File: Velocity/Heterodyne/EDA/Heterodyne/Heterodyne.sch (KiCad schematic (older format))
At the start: 35 parts, among them J3 PWR, J4 Doppler_Out, J5 V_Square, J6 OP_OUT, J7 Reciever, J8 Emmiter, U1 SA612AD, U2 NE5532, U3 MAX7375AXR105

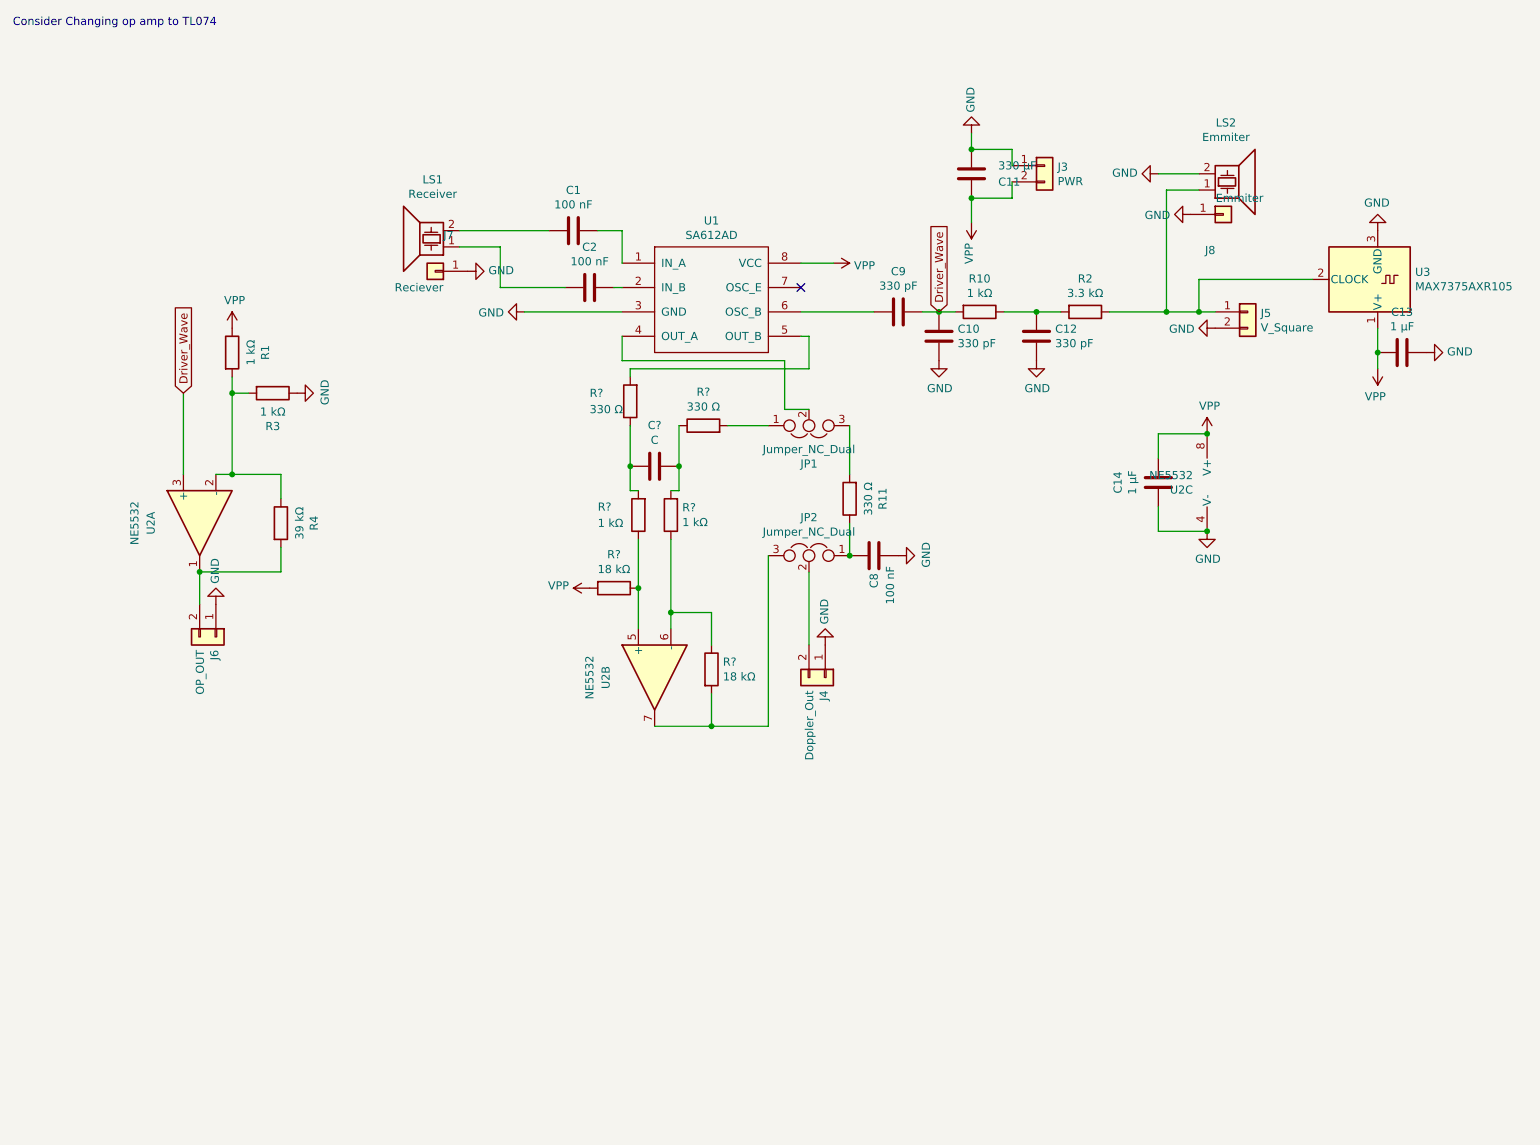
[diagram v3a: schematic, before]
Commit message: updated data to heterodyne pcb to include adc
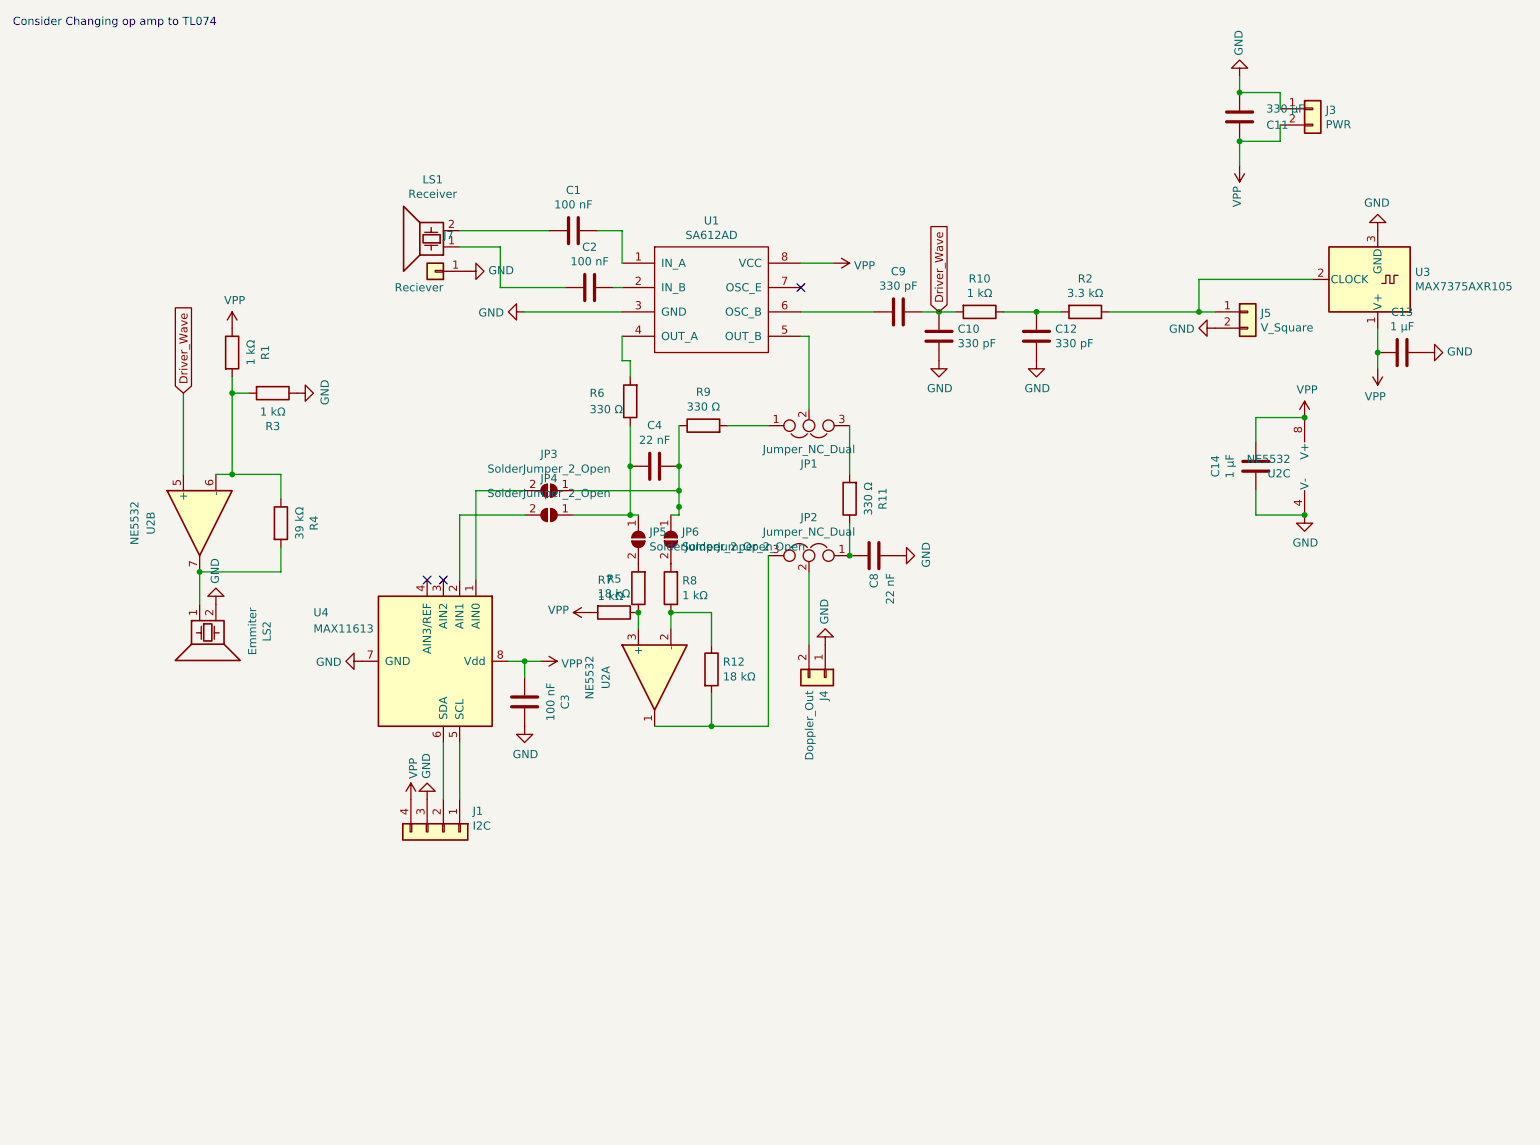
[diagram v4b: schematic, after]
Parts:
- removed J6: OP_OUT, Pin_Headers:Pin_Header_Straight_1x02_Pitch2.54mm, symbol Heterodyne-rescue:Conn_01x02-Connector_Generic
- removed J8: Emmiter, Pin_Headers:Pin_Header_Straight_1x01_Pitch2.54mm, symbol Heterodyne-rescue:Conn_01x01-Connector_Generic
- added C3: 100 nF, Capacitor_SMD:C_0805_2012Metric_Pad1.15x1.40mm_HandSolder, symbol Heterodyne-rescue:C-Device
- added J1: I2C, Connector_PinHeader_2.54mm:PinHeader_1x04_P2.54mm_Vertical, symbol Connector_Generic:Conn_01x04
- added JP3, JP4, JP5, JP6: SolderJumper_2_Open, Jumper:SolderJumper-2_P1.3mm_Open_Pad1.0x1.5mm, symbol Jumper:SolderJumper_2_Open
- added U4: MAX11613, Package_SO:MSOP-8_3x3mm_P0.65mm, symbol Analog_ADC:MAX11613
- C1, C10, C12, C2, C9: footprint Capacitors_SMD:C_0805_HandSoldering -> Capacitor_SMD:C_0805_2012Metric_Pad1.15x1.40mm_HandSolder
- C11: footprint Capacitors_SMD:CP_Elec_8x10 -> Capacitor_SMD:CP_Elec_8x10
- C13, C14: footprint Capacitors_SMD:C_1206_HandSoldering -> Capacitor_SMD:C_1206_3216Metric_Pad1.42x1.75mm_HandSolder
- C4: renamed from C?; value C -> 22 nF; footprint (none) -> Capacitor_SMD:C_0805_2012Metric_Pad1.15x1.40mm_HandSolder
- C8: value 100 nF -> 22 nF; footprint Capacitors_SMD:C_0805_HandSoldering -> Capacitor_SMD:C_0805_2012Metric_Pad1.15x1.40mm_HandSolder
- J3, J4, J5, LS1, LS2: footprint Pin_Headers:Pin_Header_Straight_1x02_Pitch2.54mm -> Connector_PinHeader_2.54mm:PinHeader_1x02_P2.54mm_Vertical
- J7: footprint Pin_Headers:Pin_Header_Straight_1x01_Pitch2.54mm -> Connector_PinSocket_2.54mm:PinSocket_1x01_P2.54mm_Vertical
- JP1, JP2: footprint Connectors:GS3 -> Jumper:SolderJumper-3_P1.3mm_Open_Pad1.0x1.5mm
- R1, R10, R11, R2, R3, R4: footprint Resistors_SMD:R_0805_HandSoldering -> Resistor_SMD:R_0805_2012Metric_Pad1.15x1.40mm_HandSolder
- R12, R5, R6, R7, R8, R9: renamed from R?; footprint (none) -> Resistor_SMD:R_0805_2012Metric_Pad1.15x1.40mm_HandSolder
- U1: footprint Housings_SOIC:SO-8_5.3x6.2mm_Pitch1.27mm -> Package_SO:SOIC-8_5.275x5.275mm_P1.27mm
- U2: footprint Housings_DIP:DIP-8_W7.62mm_LongPads -> Package_DIP:DIP-8_W7.62mm
- U3: footprint TO_SOT_Packages_SMD:SOT-323_SC-70_Handsoldering -> Package_TO_SOT_SMD:SOT-323_SC-70_Handsoldering
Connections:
- net Driver_Wave: now also U2.5 (+); no longer U2.3 (+)
- net GND: now also C3.1, J1.3 (Pin_3), U4.7 (GND)
- net VPP: now also C3.2, J1.4 (Pin_4), U4.8 (Vdd)
- net at U1.4 (OUT_A): now also R6.2; no longer JP1.2
- net at U1.5 (OUT_B): now also JP1.2; no longer R6.2
- net at J5.1 (Pin_1), R2.1, U3.2 (CLOCK): no longer LS2.1
- net at R5.1, R7.1: now also U2.3 (+); no longer U2.5 (+)
- net at R12.1, R8.1: now also U2.2 (-); no longer U2.6 (-)
- net at JP2.3, R12.2: now also U2.1; no longer U2.7
- net at R4.2: now also LS2.1, U2.7; no longer U2.1
- net at R1.2, R3.2, R4.1: now also U2.6 (-); no longer U2.2 (-)
- net at C4.2, R6.1: now also JP4.1 (A), JP5.1 (A); no longer R7.2
- net at C4.1, R9.1: now also JP3.1 (A), JP6.1 (A); no longer R8.2
- new net: JP5.2 (B), R7.2
- new net: JP6.2 (B), R8.2
- new net: JP3.2 (B), U4.1 (AIN0)
- new net: JP4.2 (B), U4.2 (AIN1)
- new net: J1.1 (Pin_1), U4.5 (SCL)
- new net: J1.2 (Pin_2), U4.6 (SDA)
- no-connect marks 1 -> 3
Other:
- moved on the sheet: C11, C14, J3, LS2, R5, R7, R8, U2C

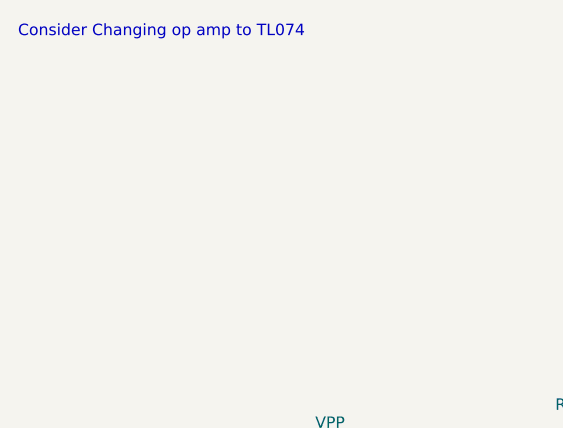
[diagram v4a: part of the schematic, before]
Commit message: calibrated velocity, implemented multi sample rate rangeing
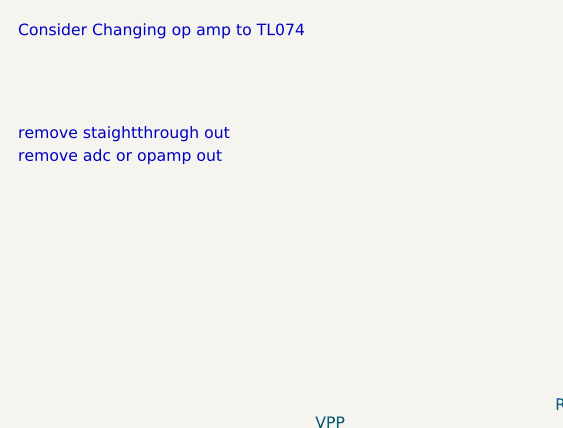
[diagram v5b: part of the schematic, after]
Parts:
- U2: footprint Package_DIP:DIP-8_W7.62mm -> Package_SO:SOIC-8_3.9x4.9mm_P1.27mm
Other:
- note added: "remove adc or opamp out\n"
- note added: "remove staightthrough out"
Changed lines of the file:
@@
 F 0 "U2" H 8863 3455 50  0000 R CNN
 F 1 "NE5532" H 8863 3544 50  0000 R CNN
-F 2 "Package_DIP:DIP-8_W7.62mm" H 9050 3500 50  0001 C CNN
+F 2 "Package_SO:SOIC-8_3.9x4.9mm_P1.27mm" H 9050 3500 50  0001 C CNN
 F 3 "http://www.ti.com/lit/ds/symlink/ne5532.pdf" H 9050 3500 50  0001 C CNN
 	3    9050 3500
@@
 F 0 "U2" H 2150 4150 50  0000 C CNN
 F 1 "NE5532" H 2150 4250 50  0000 C CNN
-F 2 "Package_DIP:DIP-8_W7.62mm" H 2150 3850 50  0001 C CNN
+F 2 "Package_SO:SOIC-8_3.9x4.9mm_P1.27mm" H 2150 3850 50  0001 C CNN
 F 3 "http://www.ti.com/lit/ds/symlink/ne5532.pdf" H 2150 3850 50  0001 C CNN
 	2    2150 3850
@@
 F 0 "U2" H 4950 5100 50  0000 C CNN
 F 1 "NE5532" H 4950 5200 50  0000 C CNN
-F 2 "Package_DIP:DIP-8_W7.62mm" H 4950 4800 50  0001 C CNN
+F 2 "Package_SO:SOIC-8_3.9x4.9mm_P1.27mm" H 4950 4800 50  0001 C CNN
 F 3 "http://www.ti.com/lit/ds/symlink/ne5532.pdf" H 4950 4800 50  0001 C CNN
 	1    4950 4800
@@
 Wire Wire Line
 	5100 3750 5100 3800
+Text Notes 1000 1250 0    50   ~ 0
+remove staightthrough out
+Text Notes 1000 1350 0    50   ~ 0
+remove adc or opamp out\n
 $EndSCHEMATC

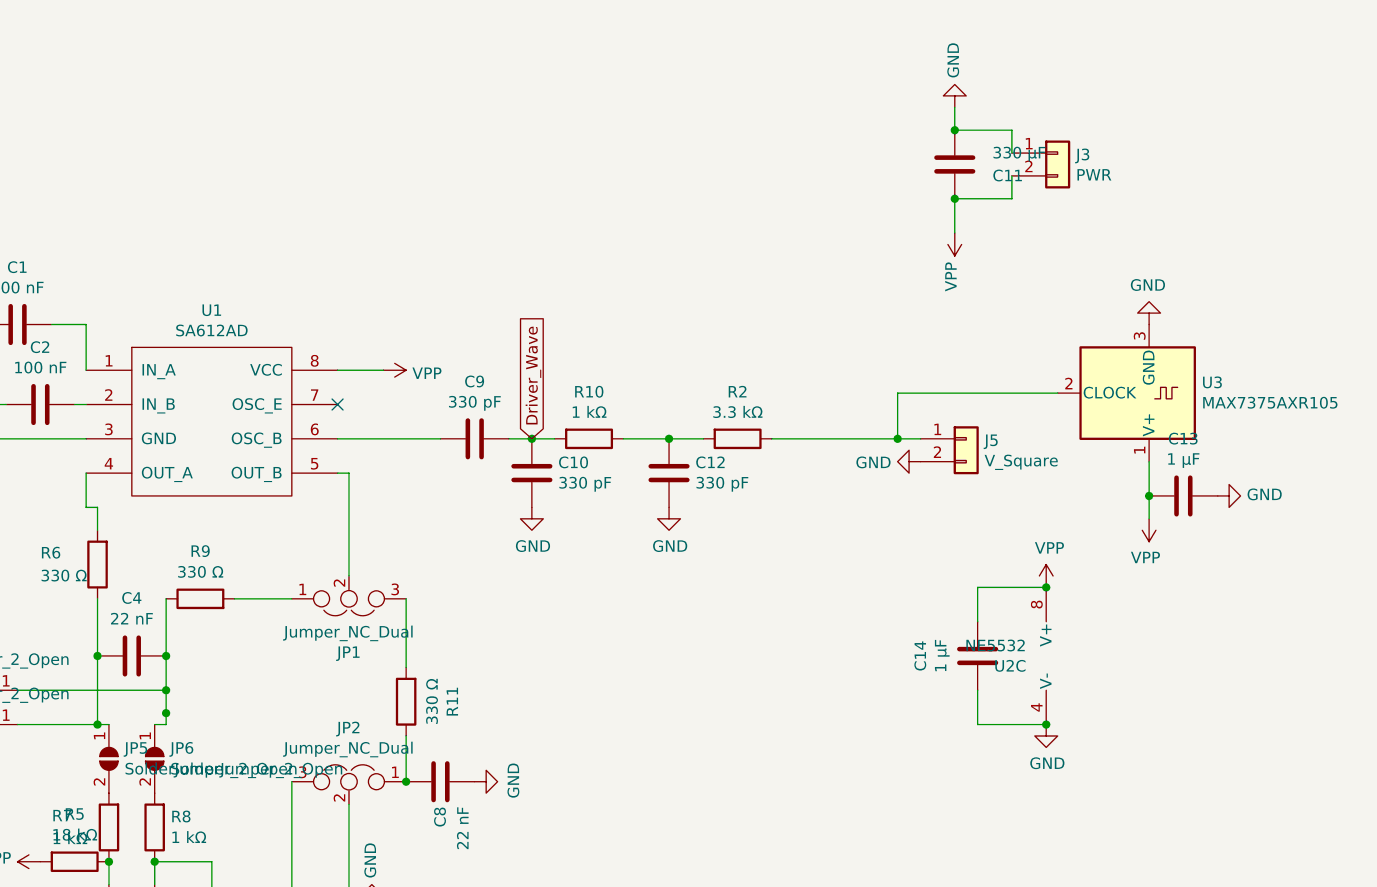
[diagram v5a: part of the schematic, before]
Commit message: added velocity testing data
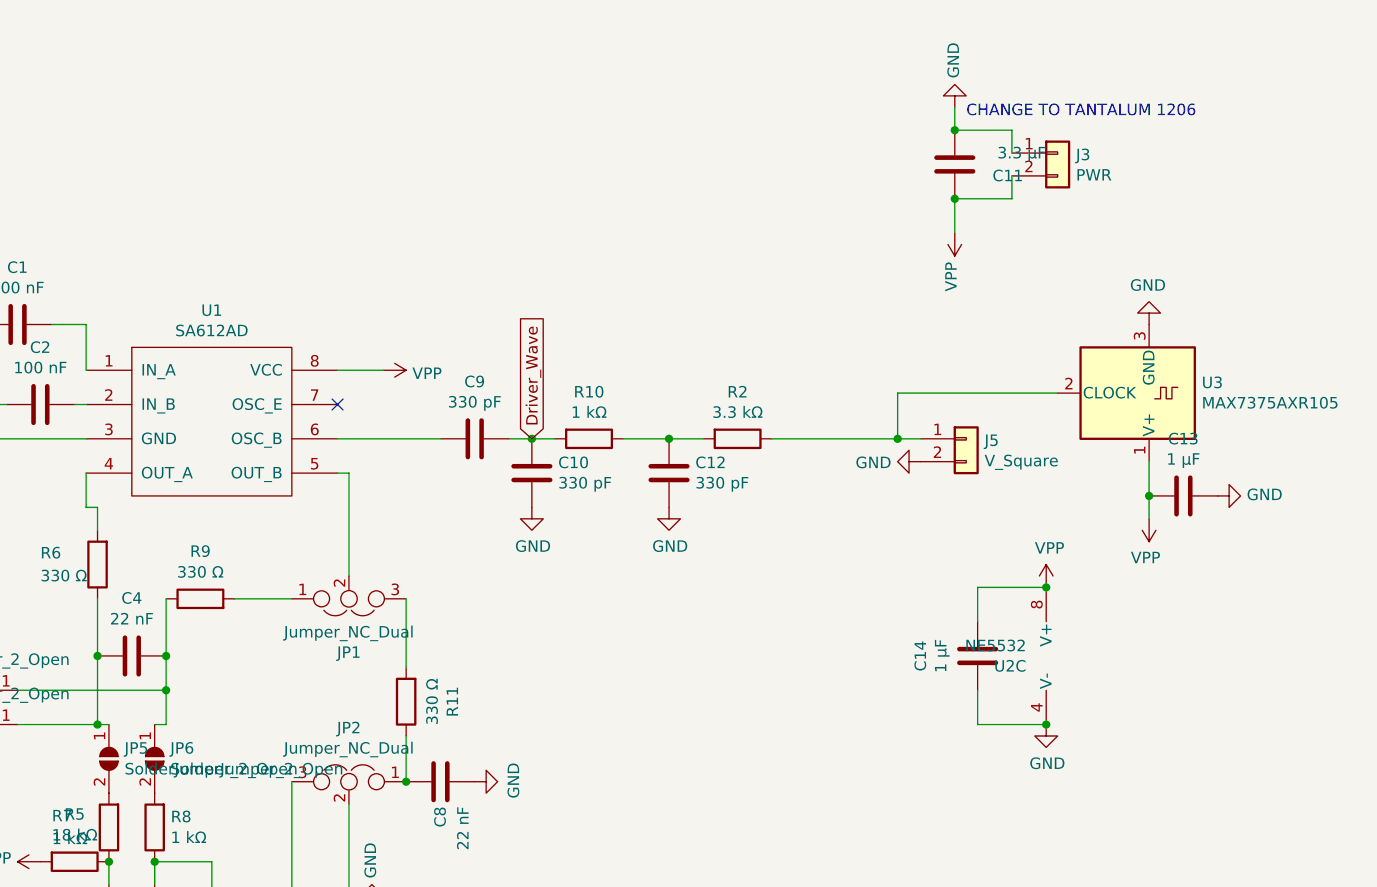
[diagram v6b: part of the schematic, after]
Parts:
- C11: value 330 μF -> 3.3 μF
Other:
- note added: "CHANGE TO TANTALUM 1206"
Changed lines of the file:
@@
 P 8550 1350
 F 0 "C11" H 8250 1400 50  0000 L CNN
-F 1 "330 μF" H 8150 1300 50  0000 L CNN
+F 1 "3.3 μF" H 8150 1300 50  0000 L CNN
 F 2 "Capacitor_SMD:CP_Elec_8x10" H 8588 1200 50  0001 C CNN
 F 3 "~" H 8550 1350 50  0001 C CNN
@@
 	5100 3500 5100 3650
 Connection ~ 5100 3650
-Wire Wire Line
-	5100 3650 5100 3750
 $Comp
 L Jumper:SolderJumper_2_Open JP4
@@
 Wire Wire Line
 	3850 3650 4150 3650
-Connection ~ 5100 3750
-Wire Wire Line
-	5100 3750 5100 3800
 Text Notes 1000 1250 0    50   ~ 0
 remove staightthrough out
 Text Notes 1000 1350 0    50   ~ 0
 remove adc or opamp out\n
+Wire Wire Line
+	5100 3650 5100 3800
+Text Notes 8600 1150 0    50   ~ 0
+CHANGE TO TANTALUM 1206
 $EndSCHEMATC
